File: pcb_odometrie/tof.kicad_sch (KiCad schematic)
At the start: 11 parts, among them J10 Conn_01x06, J11 Conn_01x06, J12 Conn_01x06, J13 Conn_01x06, J6 Conn_01x06, J7 Conn_01x06, J8 Conn_01x06, J9 Conn_01x06, U2 MCP23017T-E/SO

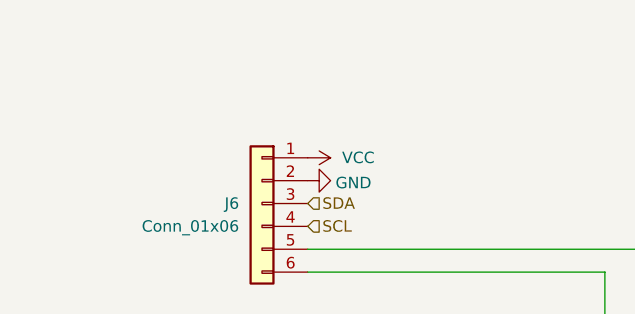
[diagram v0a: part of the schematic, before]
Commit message: ajout commentaire pcb odo
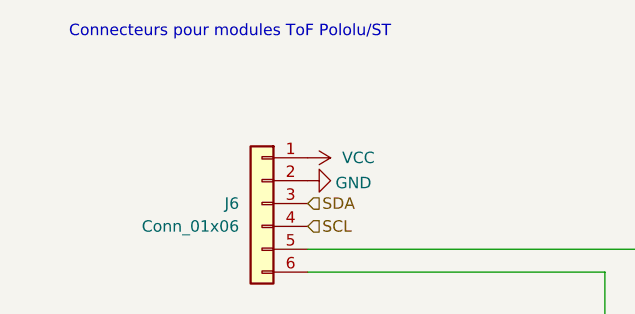
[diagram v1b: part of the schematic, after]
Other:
- note added: "Connecteurs pour modules ToF Pololu/ST"
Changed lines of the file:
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@@
 	(generator_version "9.0")
 	(paper "A4")
+	(text "Connecteurs pour modules ToF Pololu/ST"
+		(exclude_from_sim no)
+		(at 52.324 41.91 0)
+		(effects
+			(font
+				(size 1.27 1.27)
+			)
+		)
+	)
 	(junction
 		(at 121.92 62.23)

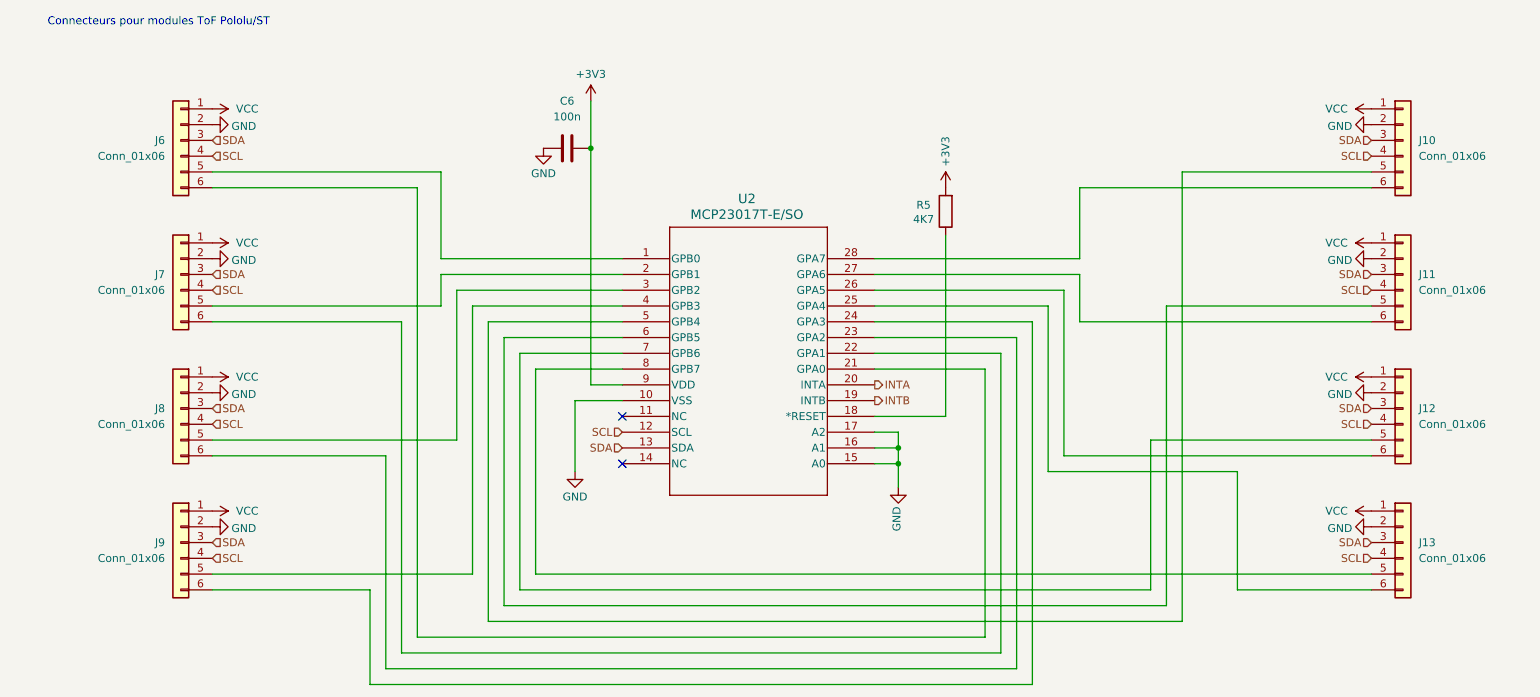
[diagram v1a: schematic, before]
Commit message: routage pcb odométrie fait : reste quelques reglages pour s'adapter au DBH-12
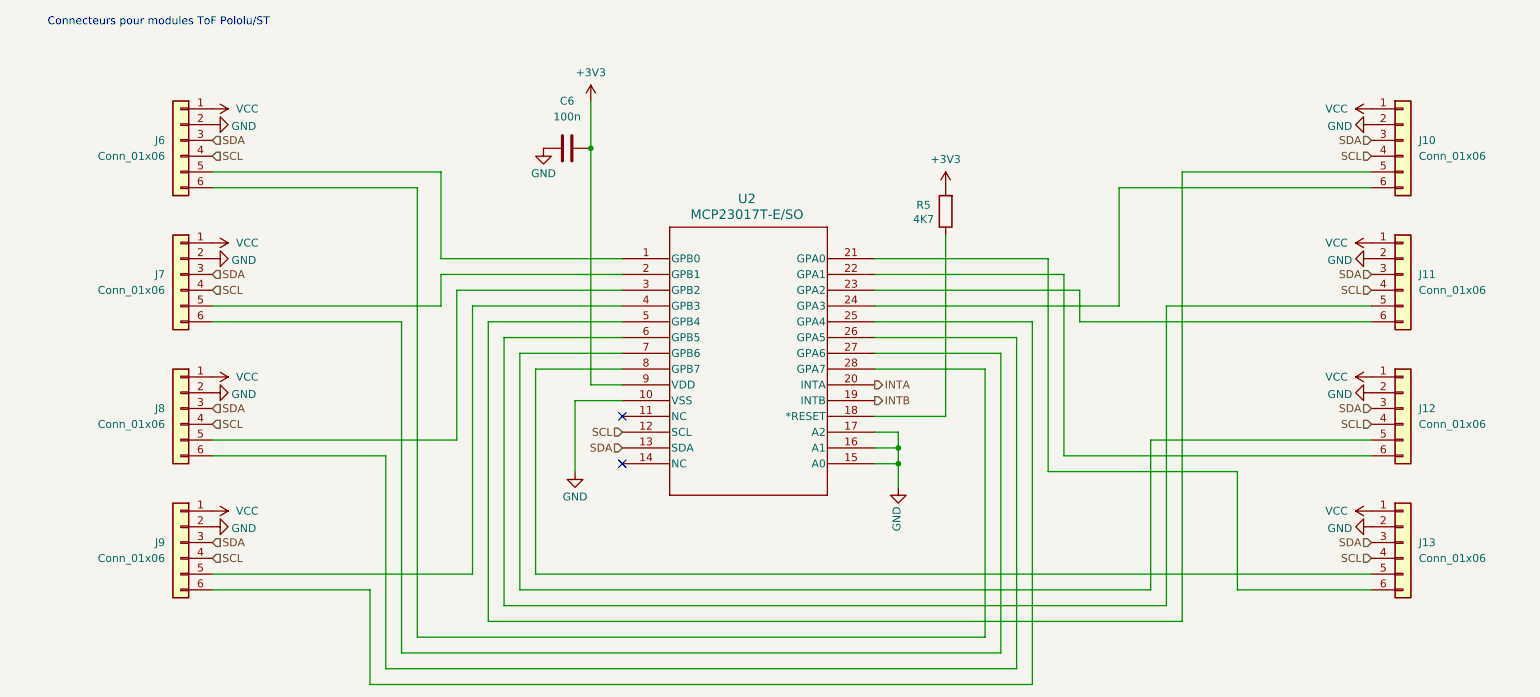
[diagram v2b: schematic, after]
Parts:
- C6: footprint (none) -> Capacitor_SMD:C_0805_2012Metric_Pad1.18x1.45mm_HandSolder
- J10, J11, J12, J13, J6, J7, J8, J9: footprint (none) -> Connector_PinHeader_1.27mm:PinHeader_1x06_P1.27mm_Vertical
- R5: footprint (none) -> Resistor_SMD:R_0805_2012Metric_Pad1.20x1.40mm_HandSolder
- U2: footprint SOIC28-W_MC_MCH -> Modelec:SOIC28-W_MC_MCH
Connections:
- net at J7.6 (Pin_6): now also U2.27 (GPA6); no longer U2.22 (GPA1)
- net at J9.6 (Pin_6): now also U2.25 (GPA4); no longer U2.24 (GPA3)
- net at J12.6 (Pin_6): now also U2.22 (GPA1); no longer U2.26 (GPA5)
- net at U2.21 (GPA0): now also J13.6 (Pin_6); no longer J6.6 (Pin_6)
- net at U2.23 (GPA2): now also J11.6 (Pin_6); no longer J8.6 (Pin_6)
- net at J10.6 (Pin_6): now also U2.24 (GPA3); no longer U2.28 (GPA7)
- new net: J8.6 (Pin_6), U2.26 (GPA5)
- new net: J6.6 (Pin_6), U2.28 (GPA7)
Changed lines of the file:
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@@
 	(wire
 		(pts
-			(xy 200.66 80.01) (xy 167.64 80.01)
+			(xy 167.64 82.55) (xy 198.12 82.55)
 		)
 		(stroke
@@
 	(wire
 		(pts
-			(xy 247.65 68.58) (xy 200.66 68.58)
+			(xy 247.65 68.58) (xy 207.01 68.58)
 		)
 		(stroke
@@
 	(wire
 		(pts
-			(xy 200.66 68.58) (xy 200.66 80.01)
+			(xy 207.01 68.58) (xy 207.01 87.63)
 		)
 		(stroke
@@
 	(wire
 		(pts
+			(xy 195.58 114.3) (xy 195.58 80.01)
+		)
+		(stroke
+			(width 0)
+			(type default)
+		)
+	)
+	(wire
+		(pts
 			(xy 226.06 133.35) (xy 226.06 114.3)
 		)
@@
 	(wire
 		(pts
-			(xy 198.12 111.76) (xy 198.12 85.09)
+			(xy 217.17 138.43) (xy 105.41 138.43)
 		)
 		(stroke
@@
 	(wire
 		(pts
-			(xy 217.17 138.43) (xy 105.41 138.43)
+			(xy 167.64 87.63) (xy 207.01 87.63)
 		)
 		(stroke
@@
 	(wire
 		(pts
+			(xy 195.58 80.01) (xy 167.64 80.01)
+		)
+		(stroke
+			(width 0)
+			(type default)
+		)
+	)
+	(wire
+		(pts
 			(xy 185.42 97.79) (xy 167.64 97.79)
 		)
@@
 	(wire
 		(pts
+			(xy 167.64 85.09) (xy 200.66 85.09)
+		)
+		(stroke
+			(width 0)
+			(type default)
+		)
+	)
+	(wire
+		(pts
 			(xy 97.79 80.01) (xy 127 80.01)
 		)
@@
 	(wire
 		(pts
-			(xy 167.64 82.55) (xy 200.66 82.55)
-		)
-		(stroke
-			(width 0)
-			(type default)
-		)
-	)
-	(wire
-		(pts
 			(xy 167.64 113.03) (xy 171.45 113.03)
 		)
@@
 	(wire
 		(pts
-			(xy 195.58 114.3) (xy 195.58 87.63)
-		)
-		(stroke
-			(width 0)
-			(type default)
-		)
-	)
-	(wire
-		(pts
 			(xy 247.65 87.63) (xy 214.63 87.63)
 		)
@@
 	(wire
 		(pts
-			(xy 200.66 90.17) (xy 200.66 82.55)
+			(xy 200.66 90.17) (xy 200.66 85.09)
 		)
 		(stroke
@@
 	(wire
 		(pts
-			(xy 198.12 85.09) (xy 167.64 85.09)
-		)
-		(stroke
-			(width 0)
-			(type default)
-		)
-	)
-	(wire
-		(pts
-			(xy 195.58 87.63) (xy 167.64 87.63)
+			(xy 60.96 111.76) (xy 88.9 111.76)
 		)
 		(stroke
@@
 	(wire
 		(pts
-			(xy 60.96 111.76) (xy 88.9 111.76)
+			(xy 198.12 82.55) (xy 198.12 111.76)
 		)
 		(stroke
@@
 			)
 		)
-		(property "Footprint" ""
+		(property "Footprint" "Connector_PinHeader_1.27mm:PinHeader_1x06_P1.27mm_Vertical"
 			(at 55.88 82.55 0)
 			(effects
@@
 			)
 		)
-		(property "Footprint" ""
+		(property "Footprint" "Connector_PinHeader_1.27mm:PinHeader_1x06_P1.27mm_Vertical"
 			(at 55.88 125.73 0)
 			(effects
@@
 		)
 		(property "Value" "+3V3"
-			(at 121.92 50.292 0)
+			(at 121.92 50.038 0)
 			(effects
 				(font
@@
 			)
 		)
-		(property "Footprint" ""
+		(property "Footprint" "Resistor_SMD:R_0805_2012Metric_Pad1.20x1.40mm_HandSolder"
 			(at 180.848 72.39 90)
 			(effects
@@
 			)
 		)
-		(property "Footprint" ""
+		(property "Footprint" "Connector_PinHeader_1.27mm:PinHeader_1x06_P1.27mm_Vertical"
 			(at 252.73 104.14 0)
 			(effects
@@
 			)
 		)
-		(property "Footprint" "SOIC28-W_MC_MCH"
+		(property "Footprint" "Modelec:SOIC28-W_MC_MCH"
 			(at 127 80.01 0)
 			(effects
@@
 			)
 		)
-		(property "Footprint" ""
+		(property "Footprint" "Connector_PinHeader_1.27mm:PinHeader_1x06_P1.27mm_Vertical"
 			(at 252.73 82.55 0)
 			(effects
@@
 			)
 		)
-		(property "Footprint" ""
+		(property "Footprint" "Capacitor_SMD:C_0805_2012Metric_Pad1.18x1.45mm_HandSolder"
 			(at 121.92 61.2648 0)
 			(effects
@@
 			)
 		)
-		(property "Footprint" ""
+		(property "Footprint" "Connector_PinHeader_1.27mm:PinHeader_1x06_P1.27mm_Vertical"
 			(at 252.73 125.73 0)
 			(effects
@@
 		)
 		(property "Value" "+3V3"
-			(at 179.07 62.738 90)
+			(at 179.07 64.008 0)
 			(effects
 				(font
@@
 			)
 		)
-		(property "Footprint" ""
+		(property "Footprint" "Connector_PinHeader_1.27mm:PinHeader_1x06_P1.27mm_Vertical"
 			(at 55.88 60.96 0)
 			(effects
@@
 			)
 		)
-		(property "Footprint" ""
+		(property "Footprint" "Connector_PinHeader_1.27mm:PinHeader_1x06_P1.27mm_Vertical"
 			(at 252.73 60.96 0)
 			(effects
@@
 			)
 		)
-		(property "Footprint" ""
+		(property "Footprint" "Connector_PinHeader_1.27mm:PinHeader_1x06_P1.27mm_Vertical"
 			(at 55.88 104.14 0)
 			(effects

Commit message: connecteur 14pin avec detrompage + renumerotation TOF
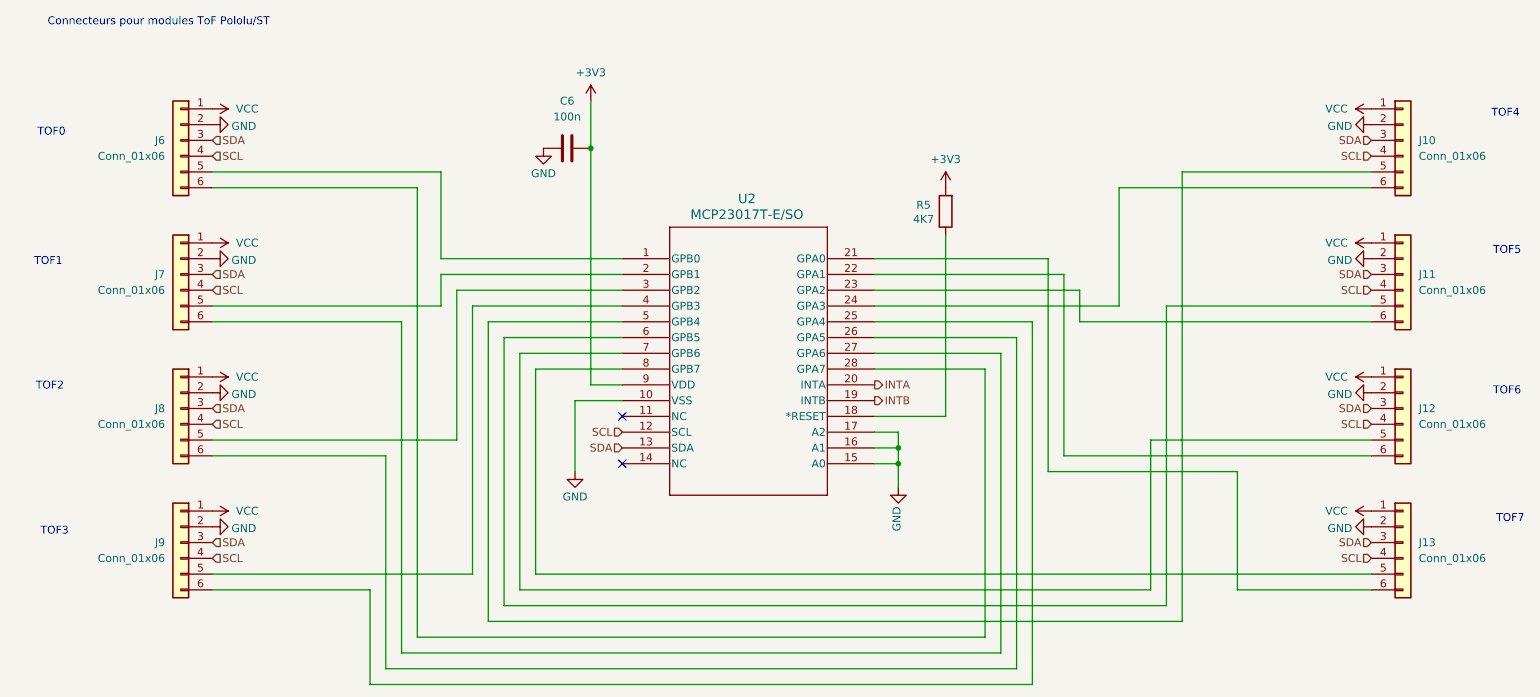
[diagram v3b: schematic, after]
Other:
- note added: "TOF0"
- note added: "TOF1"
- note added: "TOF2"
- note added: "TOF3"
- note added: "TOF4"
- note added: "TOF5"
- note added: "TOF6"
- note added: "TOF7"
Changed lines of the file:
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@@
 	(generator_version "9.0")
 	(paper "A4")
+	(text "TOF3"
+		(exclude_from_sim no)
+		(at 35.56 123.952 0)
+		(effects
+			(font
+				(size 1.27 1.27)
+			)
+		)
+	)
+	(text "TOF6"
+		(exclude_from_sim no)
+		(at 269.494 101.346 0)
+		(effects
+			(font
+				(size 1.27 1.27)
+			)
+		)
+	)
+	(text "TOF7"
+		(exclude_from_sim no)
+		(at 270.002 121.92 0)
+		(effects
+			(font
+				(size 1.27 1.27)
+			)
+		)
+	)
+	(text "TOF2"
+		(exclude_from_sim no)
+		(at 34.798 100.584 0)
+		(effects
+			(font
+				(size 1.27 1.27)
+			)
+		)
+	)
+	(text "TOF0"
+		(exclude_from_sim no)
+		(at 35.052 59.69 0)
+		(effects
+			(font
+				(size 1.27 1.27)
+			)
+		)
+	)
 	(text "Connecteurs pour modules ToF Pololu/ST"
 		(exclude_from_sim no)
@@
 		(effects
 			(font
+				(size 1.27 1.27)
+			)
+		)
+	)
+	(text "TOF1"
+		(exclude_from_sim no)
+		(at 34.544 80.518 0)
+		(effects
+			(font
+				(size 1.27 1.27)
+			)
+		)
+	)
+	(text "TOF4"
+		(exclude_from_sim no)
+		(at 269.24 56.642 0)
+		(effects
+			(font
+				(size 1.27 1.27)
+			)
+		)
+	)
+	(text "TOF5"
+		(exclude_from_sim no)
+		(at 269.494 78.74 0)
+		(effects
+			(font
